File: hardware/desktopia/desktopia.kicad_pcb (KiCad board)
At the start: 2 copper layers, 59.1 x 49.1 mm, 76 parts, among them J2 Prog_Connector, J3 USB4105GFA, J4 PowerMotor, J5 MotorCommandCon, U1 TPS5430DDA, U2 TCA9554DB, U3 ATmega32U4-A, U4 XC6206P282MR, U5 TXS0104EPW, U6 VL53L1CBV0FY_1, U7 CC6905S8-5FB005, Y1 X322516MLB4SI

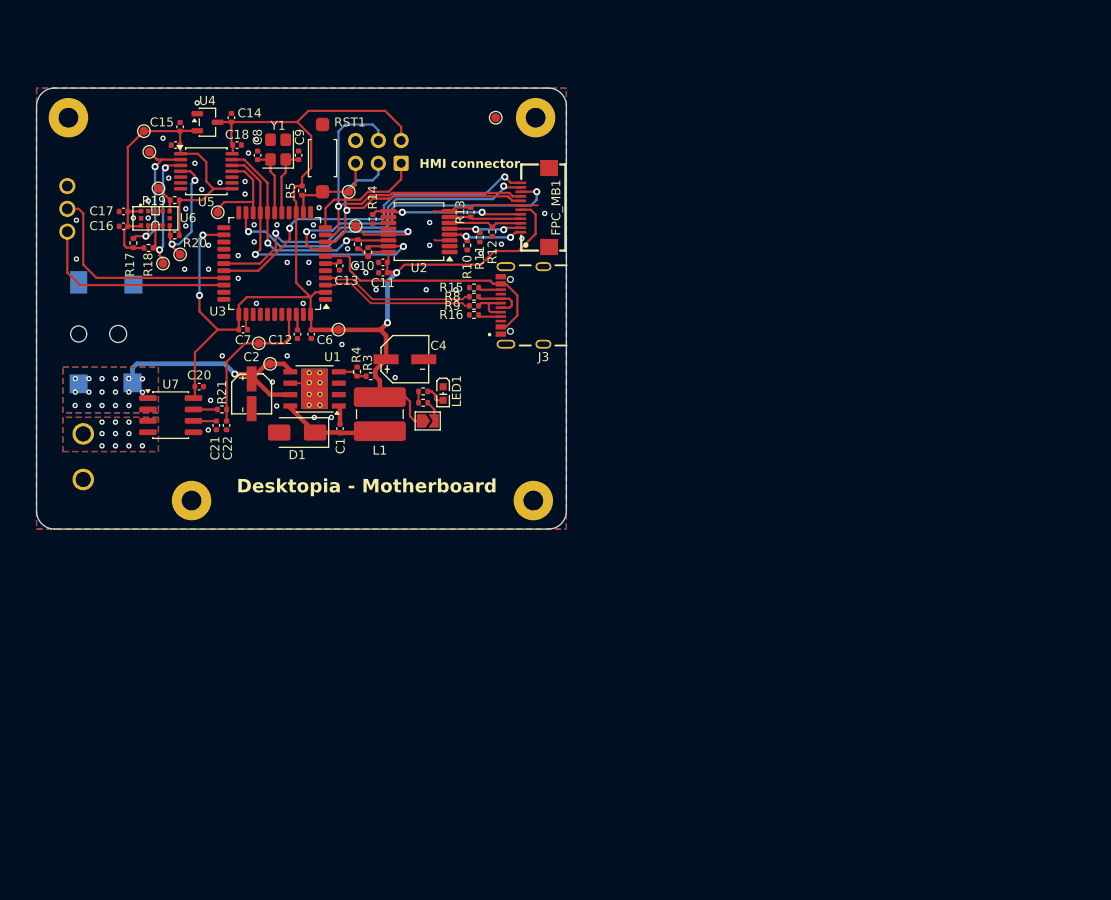
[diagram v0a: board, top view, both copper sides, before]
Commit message: hardware: motherboard PCB updated from the schematic, LCSC 3D models for the connectors
Footprints synced with the re-annotated schematic and given their 3D models. J3 and J4 use the LCSC models (VRML), U2 uses KiCad's TI_SO-PowerPAD-8. README: the J4 RJ11 jack fits its footprint, check the drilling against the datasheet.

Co-Authored-By: Claude Opus 5.5 <noreply@anthropic.com>
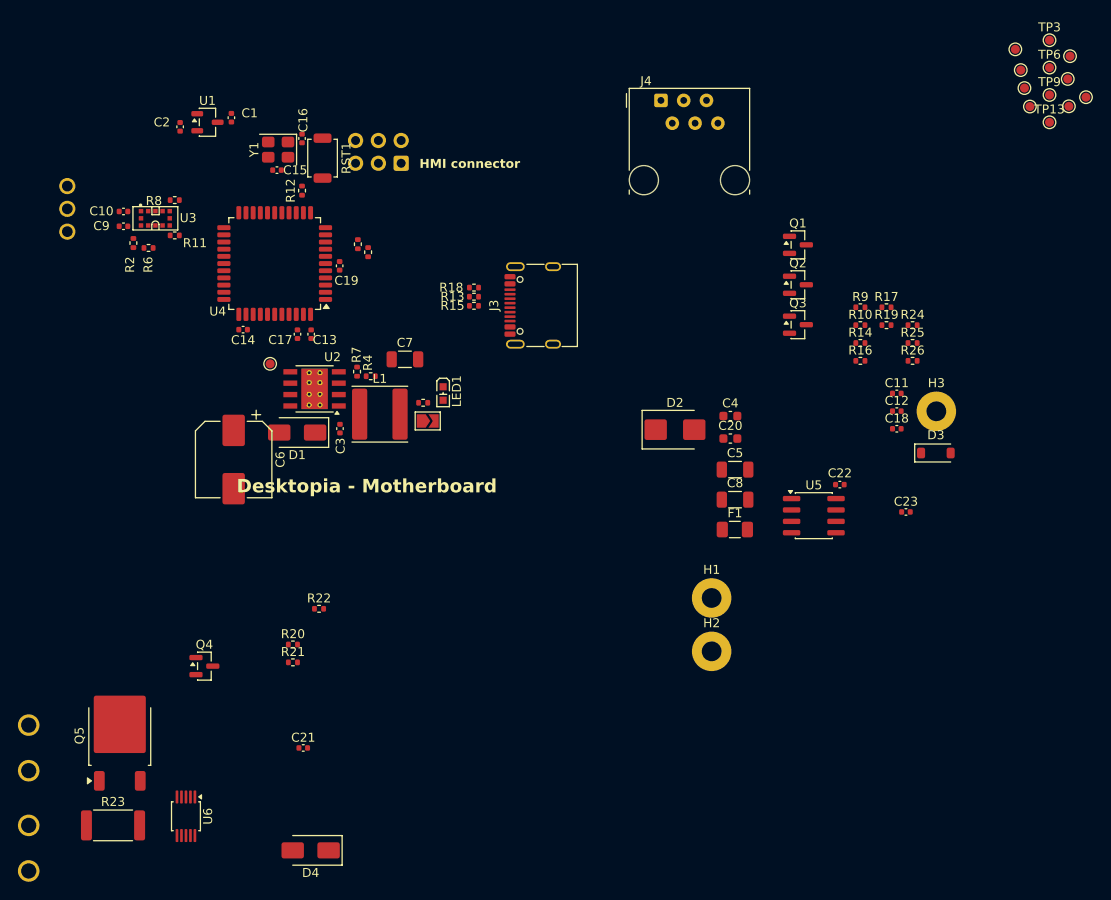
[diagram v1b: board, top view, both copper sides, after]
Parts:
- removed the C10 at (122.8, 90.6)
- removed the C19 at (99.7, 77.5)
- removed DC1: DC050-2_5-T, JLCImport:DC050-2_5-T
- removed FPC_MB1: F2D12U-A1G1-ER, JLCImport:F2D12U-A1G1-ER
- removed the H1 at (101.5, 117.1)
- removed the H1 at (139.8, 74.4)
- removed the H1 at (139.6, 117.1)
- removed the R11 at (133.6, 87.8)
- removed the R12 at (135.0, 87.1)
- removed the R13 at (132.6, 85.0)
- removed the R2 at (127.3, 104.9)
- removed TP14, TP19: TestPoint, TestPoint:TestPoint_Pad_D1.0mm
- removed the TP8 at (119.8, 86.5)
- removed the U2 at (126.8, 87.1)
- removed U7: CC6905S8-5FB005, Package_SO:SOP-8_3.76x4.96mm_P1.27mm
- added C12: 100nF, Capacitor_SMD:C_0402_1005Metric, F.Cu at (180.1, 107.1)
- added C23: 100pF, Capacitor_SMD:C_0402_1005Metric, F.Cu at (181.1, 118.4)
- added C4: 2.2nF, Capacitor_SMD:C_0603_1608Metric, F.Cu at (161.5, 107.7)
- added C5: 10uF, Capacitor_SMD:C_1206_3216Metric, F.Cu at (162.1, 113.6)
- added C8: 47uF, Capacitor_SMD:C_1206_3216Metric, F.Cu at (162.1, 117.0)
- added D2: SMBJ28A, Diode_SMD:D_SMB, F.Cu at (155.4, 109.2)
- added D3: BZT52C15, Diode_SMD:D_SOD-123, F.Cu at (184.4, 111.8)
- added D4: SS34, Diode_SMD:D_SMA, F.Cu at (114.8, 156.1)
- added F1: PTC 500mA, Fuse:Fuse_1206_3216Metric, F.Cu at (162.0, 120.3)
- added H1: MountingHole_Pad, MountingHole:MountingHole_2.2mm_M2_Pad, F.Cu at (159.4, 128.0)
- added H3: MountingHole_Pad, MountingHole:MountingHole_2.2mm_M2_Pad, F.Cu at (184.5, 107.1)
- added J1: Power24V, JLCImport:C508128L-2P0G36, B.Cu at (83.3, 155.8)
- added J4: RJ11 6P6C, Connector_RJ:RJ12_Amphenol_54601-x06_Horizontal, F.Cu at (153.8, 72.5)
- added Q1: BSS138, Package_TO_SOT_SMD:SOT-23, F.Cu at (169.1, 88.6)
- added Q2: BSS138, Package_TO_SOT_SMD:SOT-23, F.Cu at (169.1, 93.0)
- added Q3: BSS138, Package_TO_SOT_SMD:SOT-23, F.Cu at (169.1, 97.5)
- added Q4: BSS138, Package_TO_SOT_SMD:SOT-23, F.Cu at (102.9, 135.5)
- added Q5: IPD90P04P4-05, Package_TO_SOT_SMD:TO-252-2, F.Cu at (93.5, 143.3)
- added R17: 4.7k, Resistor_SMD:R_0402_1005Metric, F.Cu at (178.9, 95.6)
- added R19: 5.1k, Resistor_SMD:R_0402_1005Metric, F.Cu at (178.9, 97.5)
- added R20: 100k, Resistor_SMD:R_0402_1005Metric, F.Cu at (112.8, 133.1)
- added R22: 10k, Resistor_SMD:R_0402_1005Metric, F.Cu at (115.7, 129.2)
- added R23: 2mR 3W, Resistor_SMD:R_2512_6332Metric, F.Cu at (92.7, 153.3)
- added R24: 10k, Resistor_SMD:R_0402_1005Metric, F.Cu at (181.8, 97.5)
- added R25: 4.7k, Resistor_SMD:R_0402_1005Metric, F.Cu at (181.8, 99.5)
- added R26: 10k, Resistor_SMD:R_0402_1005Metric, F.Cu at (181.8, 101.5)
- added R9: 470, Resistor_SMD:R_0402_1005Metric, F.Cu at (176.0, 95.6)
- added TP13: TestPoint, TestPoint:TestPoint_Pad_D1.0mm, F.Cu at (197.1, 74.9)
- added TP3: TestPoint, TestPoint:TestPoint_Pad_D1.0mm, F.Cu at (197.1, 65.8)
- added TP6: TestPoint, TestPoint:TestPoint_Pad_D1.0mm, F.Cu at (197.1, 68.8)
- added TP9: TestPoint, TestPoint:TestPoint_Pad_D1.0mm, F.Cu at (197.1, 71.9)
- added U6: INA226AIDGSR, Package_SO:TSSOP-10_3x3mm_P0.5mm, F.Cu at (100.9, 152.3)
- C11: value 1uF -> 100pF
- C20: value 100nF -> 10uF; footprint Capacitor_SMD:C_0402_1005Metric -> Capacitor_SMD:C_0603_1608Metric
- C21: value 1nF -> 100nF
- C22: value 100pF -> 100nF
- C6: renamed from C2; value 4.7uF -> 100uF; footprint JLCImport:RVT1H4R7M0405_C18221489 -> Capacitor_SMD:CP_Elec_8x10
- C7: renamed from C4; value 33uF -> 47uF; footprint JLCImport:VE-330M1A0505-TRO -> Capacitor_SMD:C_1206_3216Metric
- D1: value SS14 -> SS34
- J3: value USB4105GFA -> GT-USB-7010ASV; footprint JLCImport:GCT_USB4105GFA -> Connector_USB:USB_C_Receptacle_G-Switch_GT-USB-7010ASV
- L1: value 84uH -> 22uH; footprint JLCImport:L5.8 -> Inductor_SMD:L_Sunlord_SWPA6045S
- R14: value 10k -> 4.7k
- R16: value 5.1k -> 120
- R21: value 100 -> 100k
- R3: renamed from R1; value 100 -> 470
- RST1: value SW_Push -> TS-1088-AR02016; footprint JLCImport:DTS41 -> Button_Switch_SMD:SW_SPST_TS-1088-xR020
- U5: value TXS0104EPW -> SP485EEN-L/TR; footprint Package_SO:TSSOP-14_4.4x5mm_P0.65mm -> Package_SO:SOIC-8_3.9x4.9mm_P1.27mm
- moved TP10 102.5 mm to (201.2, 72.1)
- moved TP7 102.5 mm to (199.3, 73.2)
- moved TP2 97.6 mm to (193.3, 66.8)
- moved TP4 97.6 mm to (193.9, 69.1)
- moved TP8 97.6 mm to (194.9, 73.2)
- moved H2 93.2 mm to (159.4, 133.9)
- moved TP1 87.0 mm to (199.4, 67.6)
- moved C18 80.0 mm to (180.1, 109.1)
- moved U5 77.8 mm to (170.8, 118.8)
- moved TP11 76.2 mm to (194.3, 71.1)
- moved C22 68.7 mm to (173.7, 115.3), turned to 0 degrees
- moved TP12 63.9 mm to (199.1, 70.1)
- moved C20 59.5 mm to (161.5, 110.2), turned to 0 degrees
- moved C11 58.8 mm to (180.1, 105.2)
- moved R14 56.1 mm to (176.0, 99.5), turned to 0 degrees
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- renumbered C14 to C1, C17 to C10, C6 to C13, C7 to C14, C8 to C15, C9 to C16, C12 to C17, C13 to C19, C15 to C2, C1 to C3, C16 to C9, J4 to J5, J5 to J6, R6 to R1, R20 to R11, R5 to R12, R8 to R13, R9 to R15, R15 to R18, R17 to R2, R3 to R4, R7 to R5, R18 to R6, R4 to R7, R19 to R8, TP10 to TP1, TP17 to TP10, TP7 to TP11, TP9 to TP12, TP11 to TP2, TP15 to TP4, TP1 to TP5, TP16 to TP7, TP18 to TP8, U4 to U1, U1 to U2, U6 to U3, U3 to U4
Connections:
- net /D+ renamed Net-(U4-D+)
- net /D- renamed Net-(U4-D-)
- net /MISO renamed Net-(J2-Pin_1)
- net /MOSI renamed Net-(J2-Pin_4)
- net /SCK renamed Net-(J2-Pin_3)
- C11 pad 1: GND -> Net-(U2-VSENSE)
- C11 pad 2: +5V -> GND
- C15 pad 2: Net-(U3-XTAL1) -> Net-(U4-XTAL1)
- C20 pad 1: GND -> /+5V_HMI
- C20 pad 2: +5V -> GND
- C21 pad 1: GND -> Net-(D3-A)
- C21 pad 2: Net-(U7-VREF) -> /MOTOR_SW
- C22 pad 1: GND -> +5V
- C22 pad 2: /Imotor -> GND
- J3 pad A8: unconnected-(J3-SBU1-PadA8) -> (no net)
- J3 pad B8: unconnected-(J3-SBU2-PadB8) -> (no net)
- J5 pad 1: Net-(J4-Pad1) -> /MOTOR_SW
- R10 pad 1: /SW1_MBside -> +5V
- R10 pad 2: GND -> /TOF_INT
- R11 pad 2: Net-(U5-A3) -> Net-(Q3-S)
- R14 pad 1: /SW5_MBside -> +5V
- R14 pad 2: GND -> Net-(U5-A)
- R16 pad 1: Net-(J3-CC1) -> Net-(U5-A)
- R16 pad 2: GND -> Net-(U5-B)
- R2 pad 2: Net-(U5-A1) -> Net-(Q1-S)
- R21 pad 1: Net-(U7-VOUT) -> Net-(D3-A)
- R21 pad 2: /Imotor -> /MOTOR_24V
- R3 pad 2: Net-(R1-Pad2) -> Net-(LED1-A)
- R4 pad 2: Net-(U1-VSENSE) -> Net-(U2-VSENSE)
- R6 pad 2: Net-(U5-A2) -> Net-(Q2-S)
- R7 pad 1: Net-(U1-VSENSE) -> Net-(U2-VSENSE)
- TP10 pad 1: Net-(U5-A3) -> Net-(Q3-S)
- TP4 pad 1: Net-(U5-A1) -> Net-(Q1-S)
- TP7 pad 1: Net-(U5-A2) -> Net-(Q2-S)
- U2 pad 4: Net-(U1-VSENSE) -> Net-(U2-VSENSE)
- U2 pad 5: +24V -> unconnected-(U2-EN-Pad5)
- U3 pad 10: Net-(U5-A1) -> Net-(Q1-S)
- U3 pad 7: Net-(U5-A3) -> Net-(Q3-S)
- U3 pad 9: Net-(U5-A2) -> Net-(Q2-S)
- U4 pad 1: unconnected-(U3-PE6-Pad1) -> /I_ALERT
- U4 pad 17: Net-(U3-XTAL1) -> Net-(U4-XTAL1)
- U4 pad 20: /GPIO1_VL53 -> Net-(U4-PD2)
- U4 pad 21: /HMI_~{INT} -> Net-(U4-PD3)
- U4 pad 25: unconnected-(U3-PD4-Pad25) -> Net-(U4-PD4)
- U4 pad 27: unconnected-(U3-PD7-Pad27) -> /MOTOR_PWR
- U4 pad 28: /DC_MBside -> /TOF_INT
- U4 pad 29: /RST_MBside -> unconnected-(U4-PB5-Pad29)
- U4 pad 33: GND -> unconnected-(U4-~{HWB}/PE2-Pad33)
- U4 pad 41: /Imotor -> unconnected-(U4-PF0-Pad41)
- U4 pad 7: VBUS -> Net-(U4-VBUS)
- U4 pad 8: /CS_MBside -> unconnected-(U4-PB0-Pad8)
- U5 pad 1: +2V8 -> Net-(U4-PD2)
- U5 pad 2: Net-(U5-A1) -> Net-(U4-PD4)
- U5 pad 3: Net-(U5-A2) -> Net-(U4-PD4)
- U5 pad 4: Net-(U5-A3) -> Net-(U4-PD3)
- U5 pad 5: unconnected-(U5-A4-Pad5) -> GND
- U5 pad 6: unconnected-(U5-NC-Pad6) -> Net-(U5-A)
- U5 pad 7: GND -> Net-(U5-B)
- U5 pad 8: +2V8 -> +5V
- Y1 pad 3: GND -> Net-(U4-XTAL1)
- Y1 pad 4: Net-(U3-XTAL1) -> GND
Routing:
- net +5V: track 149.3 -> 0.00 mm, vias 4 -> 0
- net +2V8: track 44.4 -> 0.00 mm
- net /DC_MBside: track 43.2 -> 0.00 mm, vias 2 -> 0
- net Net-(J2-Pin_4): track 40.0 -> 0.00 mm, vias 1 -> 0
- net /RST_MBside: track 39.4 -> 0.00 mm, vias 2 -> 0
- net Net-(J2-Pin_3): track 33.3 -> 0.00 mm, vias 1 -> 0
- net /SDA: track 33.2 -> 0.00 mm, vias 2 -> 0
- net /CS_MBside: track 30.9 -> 0.00 mm, vias 2 -> 0
- net VBUS: track 28.7 -> 0.00 mm
- net /HMI_~{INT}: track 27.7 -> 0.00 mm, vias 2 -> 0
- net +24V: track 26.3 -> 0.00 mm, vias 18 -> 0
- net /SCL: track 26.2 -> 0.00 mm, vias 2 -> 0
- net /Mpwm: track 24.0 -> 0.00 mm
- net /Mdir: track 22.6 -> 0.00 mm
- net GND: track 17.7 -> 0.00 mm, vias 55 -> 0
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- removed copper zone on B.Cu, net +24V
- removed copper zone on F.Cu, net +24V
- removed copper zone on B.Cu, net GND
- removed copper zone on F.Cu, net GND
- removed copper zone on B.Cu, net Net-(J4-Pad1)
- removed copper zone on F.Cu, net Net-(J4-Pad1)
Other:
- board outline removed
